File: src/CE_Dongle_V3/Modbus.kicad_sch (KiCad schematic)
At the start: 8 parts, among them U2 SP3485

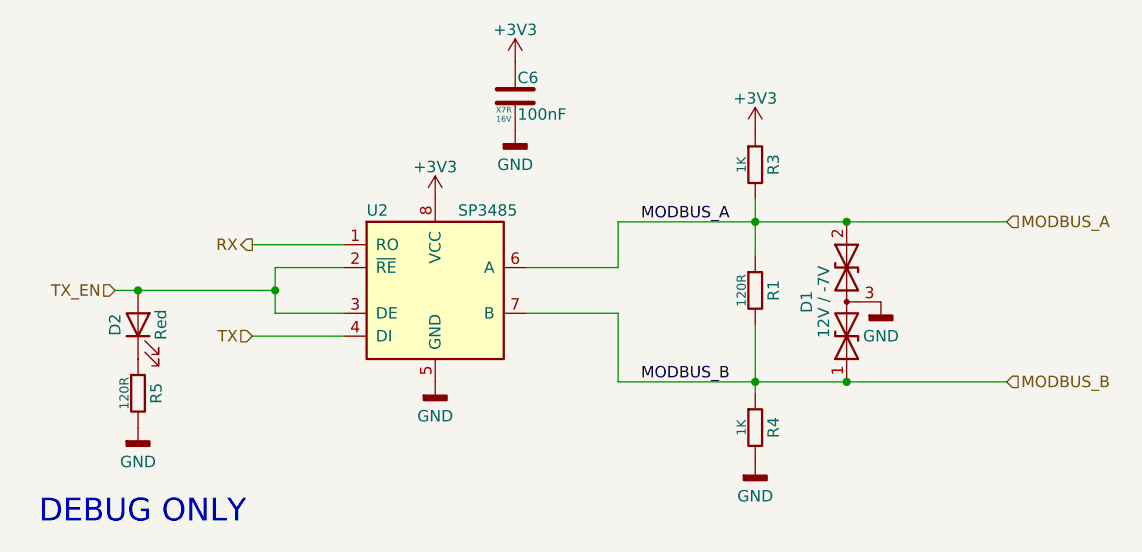
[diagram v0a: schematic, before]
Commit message: layout cont. corrected some wrong net names
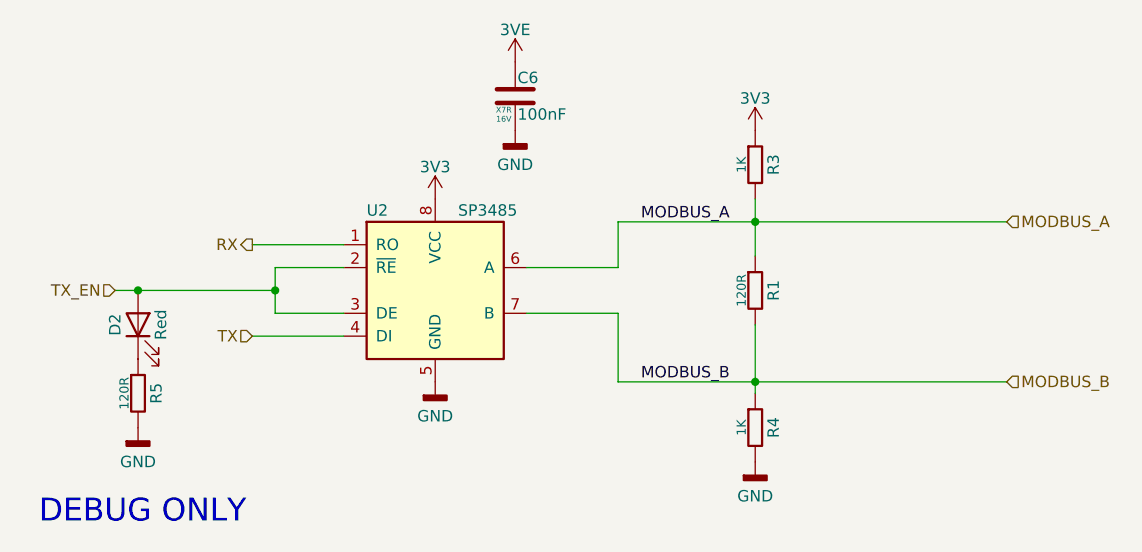
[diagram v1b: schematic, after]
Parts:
- removed D1: 12V / -7V, 7Sigma:D_SOT-23, symbol Diodes:SM712
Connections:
- net +3V3 renamed 3V3
- net 3V3: no longer C6.1
- new net 3VE: C6.1
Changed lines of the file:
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@@
-	)
-	(junction
-		(at 114.3 78.74)
-		(diameter 0)
-		(color 0 0 0 0)
 	)
 	(junction
@@
 	)
 	(junction
-		(at 114.3 60.96)
-		(diameter 0)
-		(color 0 0 0 0)
-	)
-	(junction
 		(at 104.14 60.96)
 		(diameter 0)
@@
 	(wire
 		(pts
-			(xy 114.3 60.96) (xy 132.08 60.96)
-		)
-		(stroke
-			(width 0)
-			(type default)
-		)
-	)
-	(wire
-		(pts
-			(xy 114.3 78.74) (xy 132.08 78.74)
-		)
-		(stroke
-			(width 0)
-			(type default)
-		)
-	)
-	(wire
-		(pts
 			(xy 88.9 66.04) (xy 88.9 60.96)
 		)
@@
 	(wire
 		(pts
-			(xy 114.3 78.74) (xy 104.14 78.74)
-		)
-		(stroke
-			(width 0)
-			(type default)
-		)
-	)
-	(wire
-		(pts
-			(xy 104.14 60.96) (xy 114.3 60.96)
+			(xy 104.14 78.74) (xy 132.08 78.74)
+		)
+		(stroke
+			(width 0)
+			(type default)
+		)
+	)
+	(wire
+		(pts
+			(xy 104.14 60.96) (xy 132.08 60.96)
 		)
 		(stroke
@@
 			)
 		)
-		(property "Value" "+3V3"
+		(property "Value" "3V3"
 			(at 104.14 47.244 0)
 			(effects
@@
 			)
 		)
-		(property "Value" "+3V3"
+		(property "Value" "3VE"
 			(at 77.47 39.624 0)
 			(effects
@@
 				(path "/626f6405-d1f3-452a-8480-540e5958a403/7a13ba88-4760-412d-8799-46b137fb8990"
 					(reference "#PWR01")
-					(unit 1)
-				)
-			)
-		)
-	)
-	(symbol
-		(lib_id "power:GNDD")
-		(at 118.11 69.85 0)
-		(unit 1)
-		(exclude_from_sim no)
-		(in_bom yes)
-		(on_board yes)
-		(dnp no)
-		(property "Reference" "#PWR07"
-			(at 118.11 76.2 0)
-			(effects
-				(font
-					(size 1.27 1.27)
-				)
-				(hide yes)
-			)
-		)
-		(property "Value" "GND"
-			(at 118.11 73.66 0)
-			(effects
-				(font
-					(size 1.27 1.27)
-				)
-			)
-		)
-		(property "Footprint" ""
-			(at 118.11 69.85 0)
-			(effects
-				(font
-					(size 1.27 1.27)
-				)
-				(hide yes)
-			)
-		)
-		(property "Datasheet" ""
-			(at 118.11 69.85 0)
-			(effects
-				(font
-					(size 1.27 1.27)
-				)
-				(hide yes)
-			)
-		)
-		(property "Description" "Power symbol creates a global label with name \"GNDD\" , digital ground"
-			(at 118.11 69.85 0)
-			(effects
-				(font
-					(size 1.27 1.27)
-				)
-				(hide yes)
-			)
-		)
-		(pin "1"
-		)
-		(instances
-			(project "CE_Dongle_V3"
-				(path "/626f6405-d1f3-452a-8480-540e5958a403/7a13ba88-4760-412d-8799-46b137fb8990"
-					(reference "#PWR07")
 					(unit 1)
 				)
@@
 			)
 		)
-		(property "Value" "+3V3"
+		(property "Value" "3V3"
 			(at 68.58 54.864 0)
 			(effects
@@
 					(unit 1)
 				)
-			)
-		)
-	)
-	(symbol
-		(lib_id "Diodes:SM712")
-		(at 114.3 69.85 90)
-		(unit 1)
-		(exclude_from_sim no)
-		(in_bom yes)
-		(on_board yes)
-		(dnp no)
-		(property "Reference" "D1"
-			(at 109.855 69.85 0)
-			(effects
-				(font
-					(size 1.27 1.27)
-				)
-			)
-		)
-		(property "Value" "12V / -7V"
-			(at 111.76 69.85 0)
-			(effects
-				(font
-					(size 1.27 1.27)
-				)
-			)
-		)
-		(property "Footprint" "7Sigma:D_SOT-23"
-			(at 114.3 73.66 0)
-			(effects
-				(font
-					(size 1.27 1.27)
-				)
-				(hide yes)
-			)
-		)
-		(property "Datasheet" "https://www.lcsc.com/datasheet/C502564.pdf"
-			(at 114.3 73.66 0)
-			(effects
-				(font
-					(size 1.27 1.27)
-				)
-				(hide yes)
-			)
-		)
-		(property "Description" "Asymmetrical TVS Diode for RS-485"
-			(at 114.3 69.85 0)
-			(effects
-				(font
-					(size 1.27 1.27)
-				)
-				(hide yes)
-			)
-		)
-		(property "Manufacturer 1" "MDD"
-			(at 114.3 69.85 0)
-			(effects
-				(font
-					(size 1 1)
-				)
-				(hide yes)
-			)
-		)
-		(property "Manufacturer Part Number 1" "SM712"
-			(at 114.3 69.85 0)
-			(effects
-				(font
-					(size 1 1)
-				)
-				(hide yes)
-			)
-		)
-		(property "Supplier 1" "LCSC"
-			(at 114.3 69.85 0)
-			(effects
-				(font
-					(size 1 1)
-				)
-				(hide yes)
-			)
-		)
-		(property "Supplier Part Number 1" "C502564"
-			(at 114.3 69.85 0)
-			(effects
-				(font
-					(size 1 1)
-				)
-				(hide yes)
-			)
-		)
-		(property "LCSC Part" "C502564"
-			(at 114.3 69.85 0)
-			(effects
-				(font
-					(size 1 1)
-				)
-				(hide yes)
-			)
-		)
-		(pin "1"
-		)
-		(pin "3"
-		)
-		(pin "2"
-		)
-		(instances
-			(project ""
-				(path "/626f6405-d1f3-452a-8480-540e5958a403/7a13ba88-4760-412d-8799-46b137fb8990"
-					(reference "D1")
-					(unit 1)
-				)

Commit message: layout finished
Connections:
- net 3VE is gone; now on net 3V3: C6.1
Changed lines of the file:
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@@
 			)
 		)
-		(property "Value" "3VE"
+		(property "Value" "3V3"
 			(at 77.47 39.624 0)
 			(effects
